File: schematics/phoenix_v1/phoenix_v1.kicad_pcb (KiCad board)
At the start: 2 copper layers, 11 parts, among them SW2 RotaryEncoder_Switch, U3 NHD-C0220BIZ, U5 ESP32-S3-DevKitC

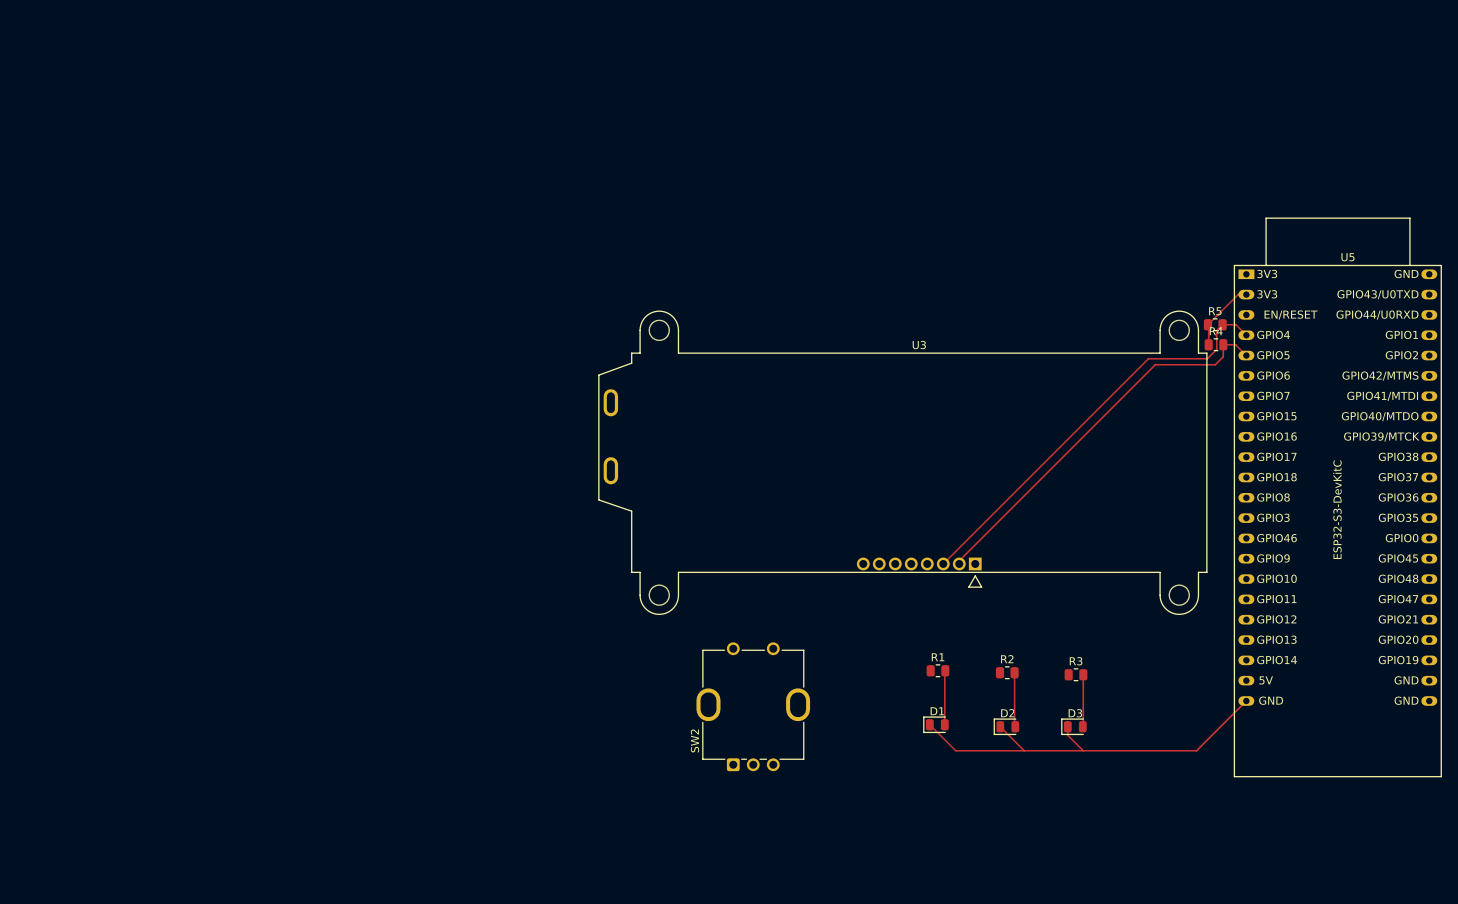
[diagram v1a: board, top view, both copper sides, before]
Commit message: finish assigning footprints and update PCB
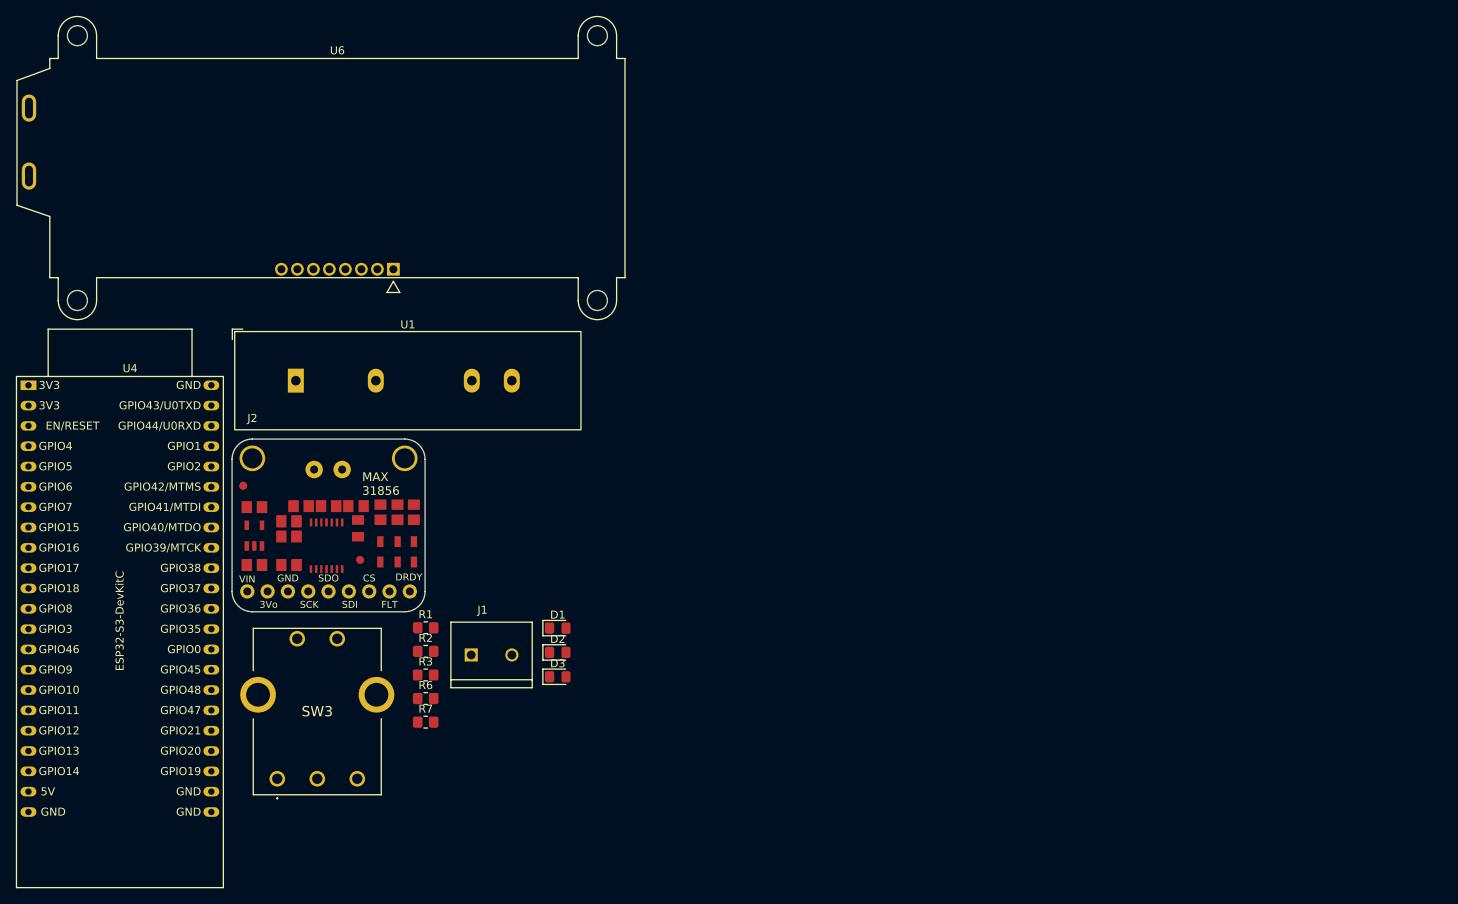
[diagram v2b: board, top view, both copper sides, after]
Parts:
- removed R4, R5: 4.7k, Resistor_SMD:R_0805_2012Metric
- removed SW2: RotaryEncoder_Switch, Rotary_Encoder:RotaryEncoder_Bourns_Vertical_PEC12R-3x17F-Sxxxx
- removed U3: NHD-C0220BIZ, Display:NHD-C0220BiZ
- removed U5: ESP32-S3-DevKitC, PCM_Espressif:ESP32-S3-DevKitC
- added J1: Screw_Terminal_01x02, phoenix_footprints:TE_282837-2, F.Cu at (96.8, 115.0)
- added J2: Conn_01x09_Socket, !footprints:MAX31856_HEADER, F.Cu at (66.9, 90.4)
- added R6: 4.7k, Resistor_SMD:R_0805_2012Metric_Pad1.20x1.40mm_HandSolder, F.Cu at (88.6, 120.5)
- added R7: 4.7k, Resistor_SMD:R_0805_2012Metric_Pad1.20x1.40mm_HandSolder, F.Cu at (88.6, 123.4)
- added SW3: RotaryEncoder_Switch, !footprints:PEC164120FS0012, F.Cu at (70.0, 130.5)
- added U1: HHG1D-1, Relay_THT:Relay_NCR_HHG1D-1, F.Cu at (72.3, 80.7)
- added U4: ESP32-S3-DevKitC, PCM_Espressif:ESP32-S3-DevKitC, F.Cu at (38.9, 81.3)
- added U6: NHD-C0220BIZ, Display:NHD-C0220BiZ, F.Cu at (77.5, 50.9)
- D1, D2, D3: footprint Diode_SMD:D_0805_2012Metric -> Diode_SMD:D_0805_2012Metric_Pad1.15x1.40mm_HandSolder
- R1, R2, R3: value 330 -> R; footprint Resistor_SMD:R_0805_2012Metric -> Resistor_SMD:R_0805_2012Metric_Pad1.20x1.40mm_HandSolder
- moved R3 81.3 mm to (88.6, 117.5)
- moved R2 72.7 mm to (88.6, 114.6)
- moved D3 65.0 mm to (105.1, 117.8)
- moved R1 64.3 mm to (88.6, 111.6)
- moved D2 57.0 mm to (105.1, 114.7)
- moved D1 49.0 mm to (105.1, 111.7)
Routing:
- net SDA: track 52.2 -> 0.00 mm
- net GND: track 51.5 -> 0.00 mm
- net SCL: track 48.9 -> 0.00 mm
- net +3.3V: track 8.99 -> 0.00 mm
- net Net-(D2-A): track 6.79 -> 0.00 mm
- net Net-(D1-A): track 6.78 -> 0.00 mm
- net Net-(D3-A): track 6.53 -> 0.00 mm
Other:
- board outline added: 24.1 x 21.6 mm

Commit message: caps for display (#21)
Co-authored-by: Waterloo Hacker Fab <waterloofab@hackerfabmacmini.uwaterloo.ca>
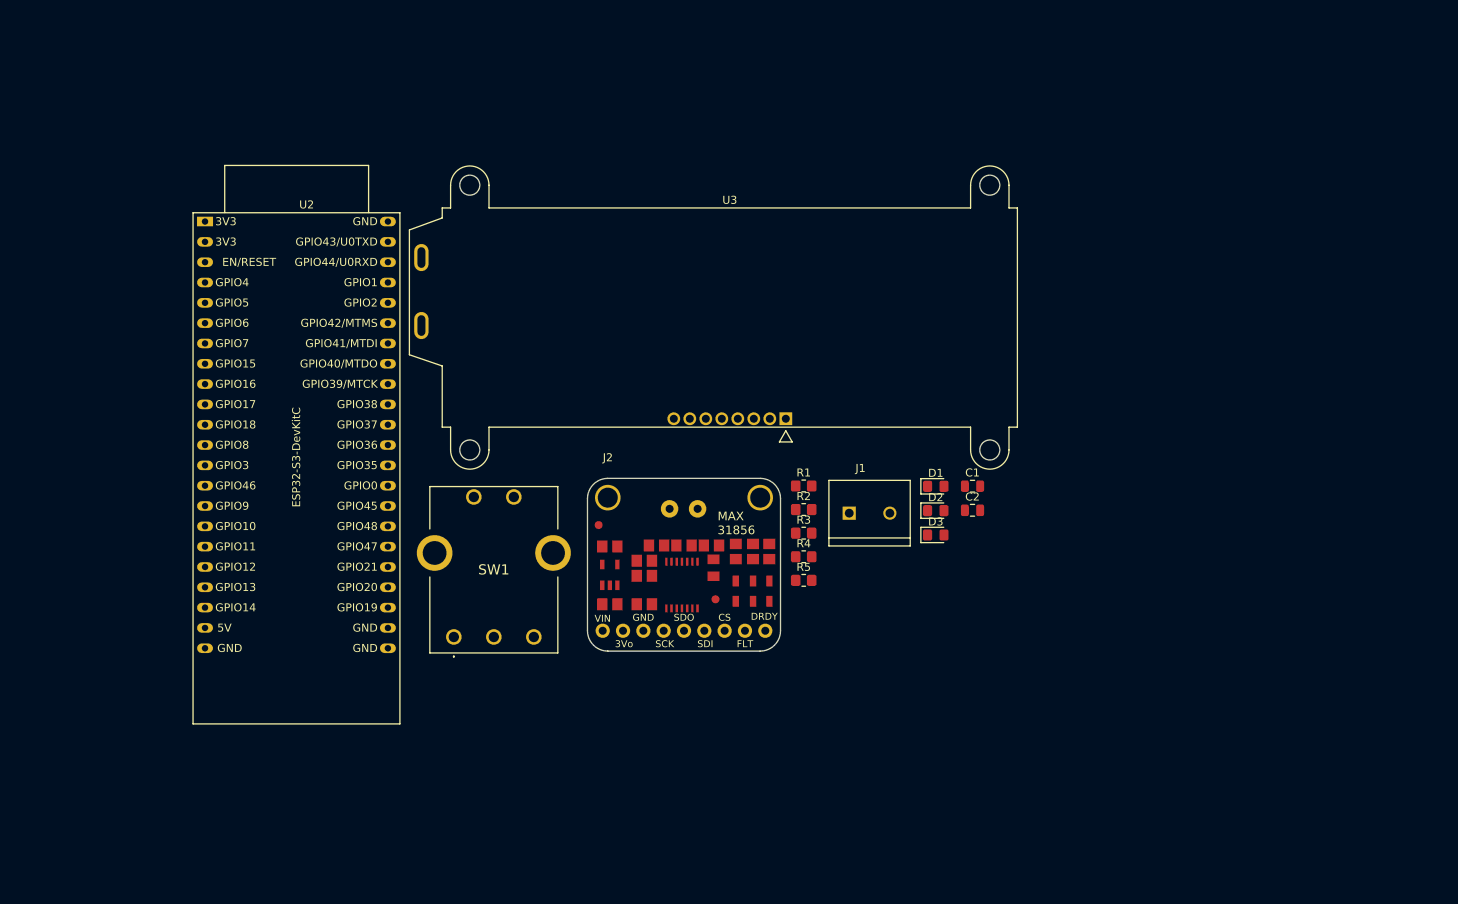
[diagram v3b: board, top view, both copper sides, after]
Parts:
- removed R6, R7: 4.7k, Resistor_SMD:R_0805_2012Metric_Pad1.20x1.40mm_HandSolder
- removed SW3: RotaryEncoder_Switch, !footprints:PEC164120FS0012
- removed U1: HHG1D-1, Relay_THT:Relay_NCR_HHG1D-1
- removed U4: ESP32-S3-DevKitC, PCM_Espressif:ESP32-S3-DevKitC
- removed U6: NHD-C0220BIZ, Display:NHD-C0220BiZ
- added C1: 1uF, Capacitor_SMD:C_0805_2012Metric, F.Cu at (156.9, 93.9)
- added C2: 1uF, Capacitor_SMD:C_0805_2012Metric, F.Cu at (156.9, 96.9)
- added R4: 4.7k, Resistor_SMD:R_0805_2012Metric_Pad1.20x1.40mm_HandSolder, F.Cu at (135.8, 102.8)
- added R5: 4.7k, Resistor_SMD:R_0805_2012Metric_Pad1.20x1.40mm_HandSolder, F.Cu at (135.8, 105.7)
- added SW1: RotaryEncoder_Switch, !footprints:PEC164120FS0012, F.Cu at (92.1, 112.8)
- added U2: ESP32-S3-DevKitC, PCM_Espressif:ESP32-S3-DevKitC, F.Cu at (61.0, 60.8)
- added U3: NHD-C0220BIZ, Display:NHD-C0220BiZ, F.Cu at (126.6, 69.6)
- R1, R2, R3: value R -> 220
- moved D1 50.5 mm to (152.3, 93.9)
- moved D2 50.5 mm to (152.3, 97.0)
- moved D3 50.5 mm to (152.3, 100.0)
- moved J1 50.5 mm to (144.0, 97.3)
- moved R1 50.5 mm to (135.8, 93.9)
- moved R2 50.5 mm to (135.8, 96.8)
- moved R3 50.5 mm to (135.8, 99.8)
- moved J2 44.7 mm to (111.3, 95.4)
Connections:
- net /VIN_1 renamed /VIN

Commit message: arrange stuff and draw outline (#25)
* show which direction MAX is facing

* arrange and draw outline

* better alignment

---------

Co-authored-by: Waterloo Hacker Fab <waterloofab@hackerfabmacmini.uwaterloo.ca>
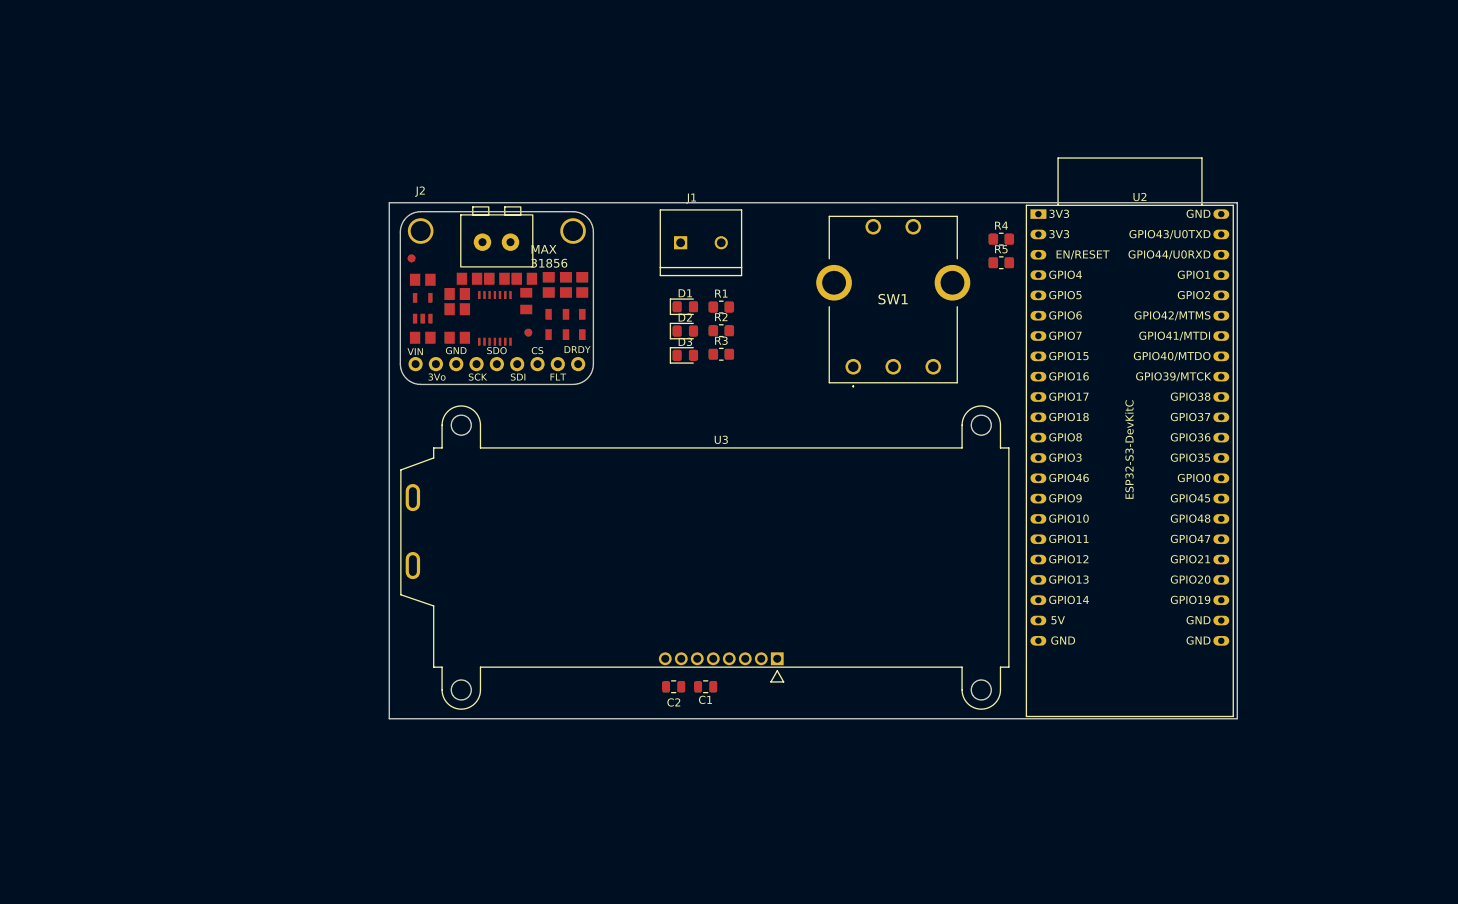
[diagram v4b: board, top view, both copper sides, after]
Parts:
- moved U2 104.2 mm to (165.1, 59.9)
- moved SW1 60.3 mm to (142.0, 79.0)
- moved R4 46.8 mm to (160.5, 63.0)
- moved R5 46.8 mm to (160.5, 66.0)
- moved C2 43.4 mm to (119.5, 119.0), turned to 180 degrees
- moved C1 41.7 mm to (123.5, 119.0), turned to 180 degrees
- moved J2 40.7 mm to (87.9, 62.0)
- moved J1 39.8 mm to (123.0, 63.5)
- moved D3 38.5 mm to (121.0, 77.6)
- moved D1 38.5 mm to (121.0, 71.5)
- moved D2 38.5 mm to (121.0, 74.5)
- moved U3 30.0 mm to (125.5, 99.6)
- moved R1 24.6 mm to (125.5, 71.5)
- moved R2 24.6 mm to (125.5, 74.5)
- moved R3 24.6 mm to (125.5, 77.4)
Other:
- board size 24.1 x 21.6 mm -> 106 x 64.5 mm

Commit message: fix encoder footprint and label mismatch
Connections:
- U2 pad 33: ENC_A -> /ENC_A
- U2 pad 34: ENC_B -> /ENC_B
- U2 pad 35: ENC_SW -> /ENC_SW

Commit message: update on pcb
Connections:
- net /VIN renamed /VIN_1
